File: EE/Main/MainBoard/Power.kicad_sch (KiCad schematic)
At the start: 31 parts, among them J8 Conn_01x02_Male, P1 USB_C_Plug_USB2.0, SW1 EG1206A, U2 LM3670MF-3.3, U4 MCP73832-2-OT, U5 MCP1640Cx-xCHY

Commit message: First pass layout
Assumes using Cut-through RGB 7 Segment
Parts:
- renumbered TP+ to TP+1, TP- to TP-1, TPVBAT to TPVBAT1, TPVBUS to TPVBUS1, TPVCC to TPVCC1, TPVd to TPVd1
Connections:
- net V_PRE_REG renamed VBAT_ADC
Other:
- note removed: "TODO Need to boost back up to 3.9V"
- note removed: "TODO math for resistors"
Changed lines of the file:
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@@
 		)
 	)
-	(text "TODO Need to boost back up to 3.9V"
-		(exclude_from_sim no)
-		(at 233.934 82.55 0)
-		(effects
-			(font
-				(size 1.27 1.27)
-			)
-		)
-	)
 	(text "Regulators"
 		(exclude_from_sim no)
@@
 		)
 	)
-	(text "TODO math for resistors"
-		(exclude_from_sim no)
-		(at 245.872 149.098 0)
-		(effects
-			(font
-				(size 1.27 1.27)
-			)
-		)
-	)
 	(label "VBAT"
 		(at 66.04 84.582 0)
@@
 		)
 	)
-	(label "V_DISPLAY"
-		(at 269.24 18.542 180)
+	(label "V_PRE_REG"
+		(at 138.43 81.28 0)
+		(fields_autoplaced yes)
+		(effects
+			(font
+				(size 1.27 1.27)
+			)
+			(justify left bottom)
+		)
+	)
+	(label "ADC_"
+		(at 270.51 24.13 180)
 		(fields_autoplaced yes)
 		(effects
@@
 		)
 	)
+	(label "ADC_"
+		(at 138.43 81.28 180)
+		(fields_autoplaced yes)
+		(effects
+			(font
+				(size 1.27 1.27)
+			)
+			(justify right bottom)
+		)
+	)
 	(label "VBAT"
 		(at 151.13 128.27 270)
@@
 		)
 	)
-	(hierarchical_label "V_DISPLAY"
+	(hierarchical_label "VBAT_ADC"
 		(shape input)
-		(at 269.24 18.542 0)
+		(at 270.51 24.13 0)
 		(fields_autoplaced yes)
 		(effects
@@
 		(dnp no)
 		(fields_autoplaced yes)
-		(property "Reference" "TP+"
+		(property "Reference" "TP+1"
 			(at 142.748 122.2205 90)
 			(effects
@@
 			(project ""
 				(path "/dfe0084c-a900-4f47-8966-915ebf3a8e75/d7ae3dec-973e-4961-81aa-d99c06a6b362"
-					(reference "TP+")
+					(reference "TP+1")
 					(unit 1)
 				)
@@
 		(on_board yes)
 		(dnp no)
-		(property "Reference" "TPVd"
+		(property "Reference" "TPVd1"
 			(at 274.574 106.934 0)
 			(effects
@@
 			(project "MainBoard"
 				(path "/dfe0084c-a900-4f47-8966-915ebf3a8e75/d7ae3dec-973e-4961-81aa-d99c06a6b362"
-					(reference "TPVd")
+					(reference "TPVd1")
 					(unit 1)
 				)
@@
 		(on_board yes)
 		(dnp no)
-		(property "Reference" "TPVCC"
+		(property "Reference" "TPVCC1"
 			(at 249.174 37.084 0)
 			(effects
@@
 			(project "MainBoard"
 				(path "/dfe0084c-a900-4f47-8966-915ebf3a8e75/d7ae3dec-973e-4961-81aa-d99c06a6b362"
-					(reference "TPVCC")
+					(reference "TPVCC1")
 					(unit 1)
 				)
@@
 		(dnp no)
 		(fields_autoplaced yes)
-		(property "Reference" "TP-"
+		(property "Reference" "TP-1"
 			(at 162.179 115.6278 90)
 			(effects
@@
 			(project ""
 				(path "/dfe0084c-a900-4f47-8966-915ebf3a8e75/d7ae3dec-973e-4961-81aa-d99c06a6b362"
-					(reference "TP-")
+					(reference "TP-1")
 					(unit 1)
 				)
@@
 		(dnp no)
 		(fields_autoplaced yes)
-		(property "Reference" "TPVBUS"
+		(property "Reference" "TPVBUS1"
 			(at 41.529 59.7478 90)
 			(effects
@@
 			(project "MainBoard"
 				(path "/dfe0084c-a900-4f47-8966-915ebf3a8e75/d7ae3dec-973e-4961-81aa-d99c06a6b362"
-					(reference "TPVBUS")
+					(reference "TPVBUS1")
 					(unit 1)
 				)
@@
 		(dnp no)
 		(fields_autoplaced yes)
-		(property "Reference" "TPVBAT"
+		(property "Reference" "TPVBAT1"
 			(at 77.089 59.7478 90)
 			(effects
@@
 			(project "MainBoard"
 				(path "/dfe0084c-a900-4f47-8966-915ebf3a8e75/d7ae3dec-973e-4961-81aa-d99c06a6b362"
-					(reference "TPVBAT")
+					(reference "TPVBAT1")
 					(unit 1)
 				)

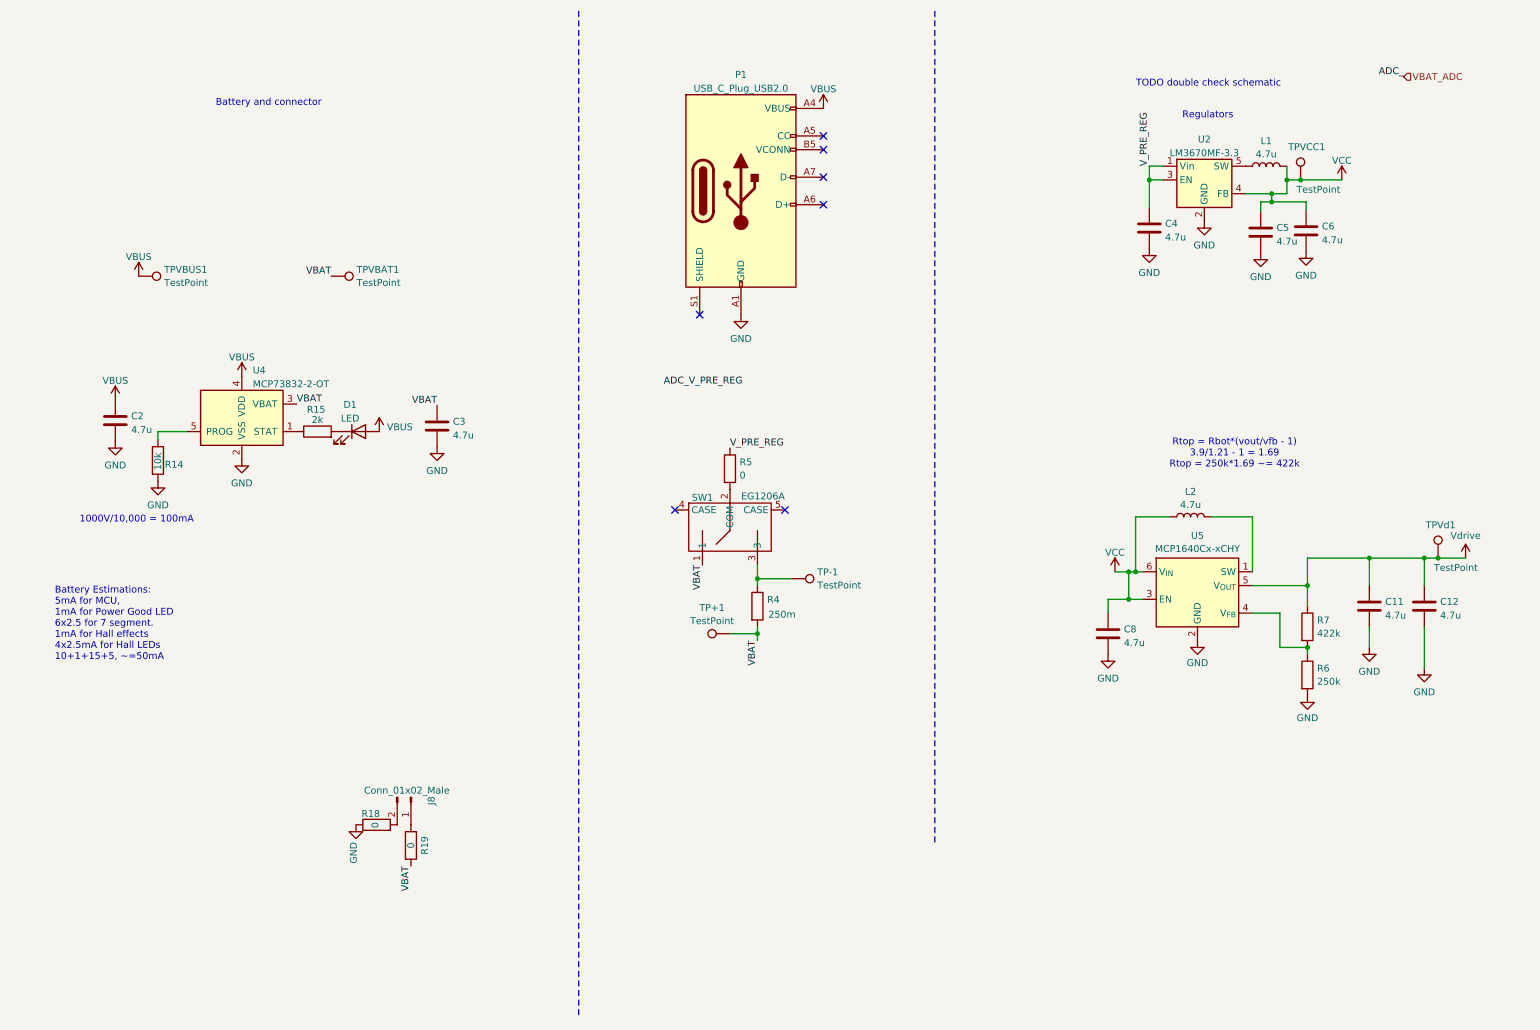
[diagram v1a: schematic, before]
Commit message: MCU Modification
Migrated to g431, as is used elsewhere.
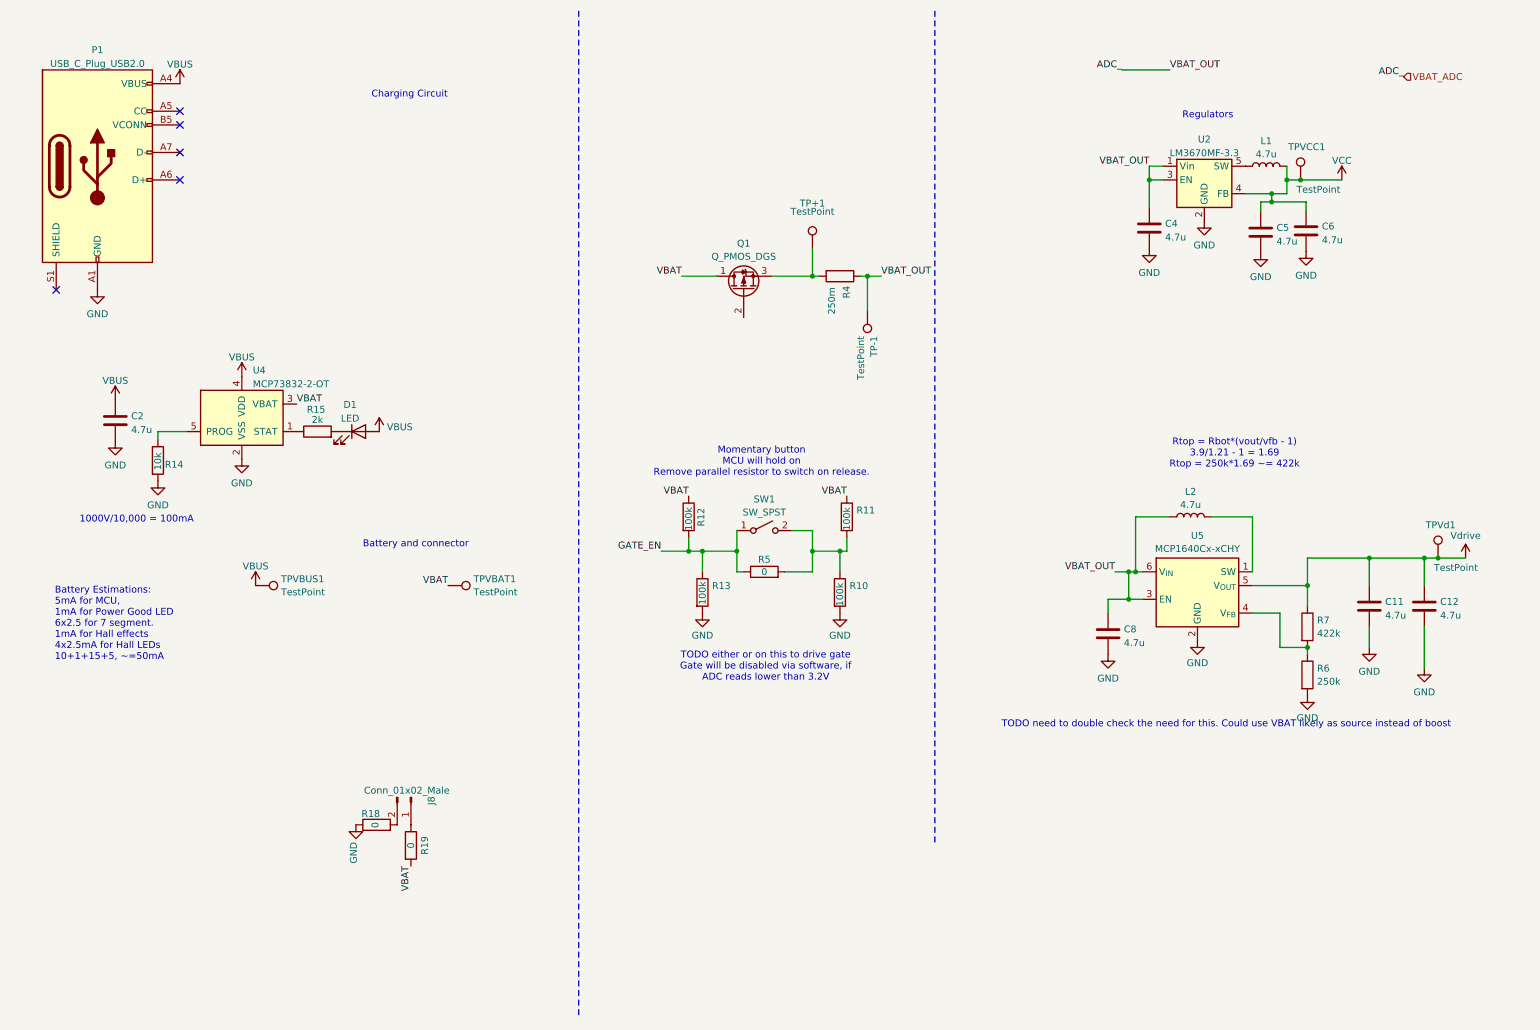
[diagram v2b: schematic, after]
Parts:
- removed C3: 4.7u, Capacitor_SMD:C_0603_1608Metric, symbol Device:C
- removed SW1: EG1206A, Library:EG1206A_EWI, symbol New_Library:EG1206A
- added Q1: Q_PMOS_DGS, symbol Device:Q_PMOS_DGS
- added R10, R11, R12, R13: 100k, symbol Device:R
- added SW1: SW_SPST, symbol Switch:SW_SPST
- R5: footprint Resistor_SMD:R_0402_1005Metric_Pad0.72x0.64mm_HandSolder -> (none)
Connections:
- net GND: now also R10.2, R13.2
- net VBAT: now also Q1.1 (D), R11.1, R12.1; no longer R4.2, TP+1.1
- net VBAT_ADC: now also C8.1, L2.1, R4.1, TP-1.1, U5.3 (EN), U5.6 (V_{IN}); no longer R5.1
- net VCC: no longer C8.1, L2.1, U5.3 (EN), U5.6 (V_{IN})
- net at R5.2: now also R10.1, R11.2, SW1.2 (B)
- new net: Q1.3 (S), R4.2, TP+1.1
- new net GATE_EN: R12.2, R13.1, R5.1, SW1.1 (A)
- no-connect marks 7 -> 5
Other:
- note added: "Charging Circuit"
- note added: "Momentary button MCU will hold on Remove parallel resistor to switch on release."
- note added: "TODO either or on this to drive gate Gate will be disabled via software, if ADC reads lower than 3.2V"
- note added: "TODO need to double check the need for this. Could use VBAT likely as source instead of boost"
- note removed: "TODO double check schematic"
- moved on the sheet: P1, R4, TP+1, TP-1, TPVBAT1, TPVBUS1

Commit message: Routine Checkout
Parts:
- removed C12: 4.7u, Capacitor_SMD:C_0603_1608Metric, symbol Device:C
- removed Q1: Q_PMOS_DGS, symbol Device:Q_PMOS_DGS
- removed R19: 0, Resistor_SMD:R_0402_1005Metric, symbol Device:R
- removed SW1: SW_SPST, symbol Switch:SW_SPST
- removed TPVBAT1, TPVBUS1, TPVd1: TestPoint, TestPoint:TestPoint_Pad_1.5x1.5mm, symbol Connector:TestPoint
- removed U2: LM3670MF-3.3, Package_TO_SOT_SMD:TSOT-23-5, symbol Regulator_Switching:LM3670MF
- removed U4: MCP73832-2-OT, Package_TO_SOT_SMD:SOT-23-5, symbol Battery_Management:MCP73832-2-OT
- removed U5: MCP1640Cx-xCHY, Package_TO_SOT_SMD:SOT-23-6, symbol Regulator_Switching:MCP1640Cx-xCHY
- added Q1: Q_PMOS_GSD, Package_TO_SOT_SMD:SOT-23, symbol Device:Q_PMOS_GSD
- added Q2: Q_NMOS_GSD, Package_TO_SOT_SMD:SOT-23, symbol Device:Q_NMOS_GSD
- added R21, R22: 10k, Resistor_SMD:R_0402_1005Metric, symbol Device:R
- added R23: 550k, Resistor_SMD:R_0402_1005Metric, symbol Device:R
- added R24: 100k, Resistor_SMD:R_0402_1005Metric, symbol Device:R
- added R25, R26: 1M, Resistor_SMD:R_0402_1005Metric, symbol Device:R
- added SW1: SW_DPST, symbol Switch:SW_DPST
- added TP3v1, TPPGate1: TestPoint, TestPoint:TestPoint_Pad_1.5x1.5mm, symbol Connector:TestPoint
- added U2: MCP73832-2-OT, Package_TO_SOT_SMD:SOT-23-5, symbol Battery_Management:MCP73832-2-OT
- added U4: ~, Package_TO_SOT_SMD:SOT-583-8, symbol library:TPS61033
- added U5: LM3670MF-3.3, Package_TO_SOT_SMD:TSOT-23-5, symbol Regulator_Switching:LM3670MF
- L1: value 4.7u -> 0.47u; P/N 74479775222A -> (none)
- R10, R13: value 100k -> 10k; footprint (none) -> Resistor_SMD:R_0402_1005Metric
- R11: value 100k -> 0; footprint (none) -> Resistor_SMD:R_0402_1005Metric
- R12: value 100k -> 250m; footprint (none) -> Resistor_SMD:R_0805_2012Metric
- R15: value 2k -> 10K
- R18: value 0 -> 10K
- R4: value 250m -> 10k; footprint Resistor_SMD:R_0805_2012Metric -> Resistor_SMD:R_0402_1005Metric
- R5: value 0 -> 4.7k; footprint (none) -> Resistor_SMD:R_0402_1005Metric
- R6: value 250k -> 1M; footprint (none) -> Resistor_SMD:R_0402_1005Metric
- R7: value 422k -> 0; footprint (none) -> Resistor_SMD:R_0402_1005Metric
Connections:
- net GATE_EN: now also R6.2, Q1.1 (G), Q2.3 (D), SW1.3, TPPGate1.1; no longer R12.2, R13.1, R5.1
- net GND: now also C5.1, R4.2, R7.1, R21.2, R24.2, R25.2, R26.2, U2.2 (VSS), U4.6 (GND), U5.2 (GND); no longer C5.2, R18.1, R6.2
- net VBAT: now also R11.2, R6.1, Q1.2 (S), U2.3 (VBAT); no longer R11.1, R12.1
- net VBAT_ADC: now also C5.2, L1.1, R12.1, U4.1 (VIN), U5.1 (Vin), U5.3 (EN); no longer C8.1, L2.1, R4.1
- net VBUS: now also U2.4 (VDD)
- net at J8.2 (Pin_2): now also R7.2; no longer R18.2
- net P_DRAIN: now reaches TP+1.1
- net P_DRAIN: now also R12.2, Q1.3 (D); no longer R4.2
- net at D1.1 (K): now also R5.2; no longer R15.2
- net N_SOURCE: now reaches R14.1
- net N_SOURCE: now also Q2.2 (S)
- net +3V3: now reaches L2.2
- net +3V3: now also C6.1, C8.1, R15.1, R18.1, TPVCC1.1, R25.1, SW1.1, U5.4 (FB)
- net at J8.1 (Pin_1): now also R11.1
- removed net VCC: C5.1, C6.1, L1.2, TPVCC1.1
- net Vdrive renamed 3v9
- net 3v9: now also R22.1, R23.1, R26.1, TP3v1.1, U4.8 (VOUT); no longer R7.1
- new net: R23.2, R24.1, U4.5 (FB)
- new net: L2.1, U5.5 (SW)
- new net: R22.2, U4.4 (PG)
- new net: R10.1, SW1.4
- new net: R4.1, U2.5 (PROG)
- new net: R5.1, U2.1 (STAT)
- new net: L1.2, U4.7 (SW)
- new net BTN_SNS: SW1.2
- new net EN: R18.2, U4.2 (EN)
- new net MODE: R21.1, U4.3 (MODE)
- new net N_GATE: Q2.1 (G), R13.1, R15.2
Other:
- note added: "R20= (Vout/vref-1)*R19 R20= (3.9/0.6-1)*100k R20 = 550k"
- note removed: "1000V/10,000 = 100mA"
- note removed: "Battery Estimations: 5mA for MCU, 1mA for Power Good LED 6x2.5 for 7 segment. 1mA for Hall effects 4x2.5mA for Hall LEDs 10+1+15+5, ~=50mA"
- note removed: "Battery and connector"
- note removed: "Charging Circuit"
- note removed: "Regulators"
- note removed: "Rtop = Rbot*(vout/vfb - 1) 3.9/1.21 - 1 = 1.69 Rtop = 250k*1.69 ~= 422k"
- note removed: "TODO either or on this to drive gate Gate will be disabled via software, if ADC reads lower than 3.2V"
- note removed: "TODO need to double check the need for this. Could use VBAT likely as source instead of boost"

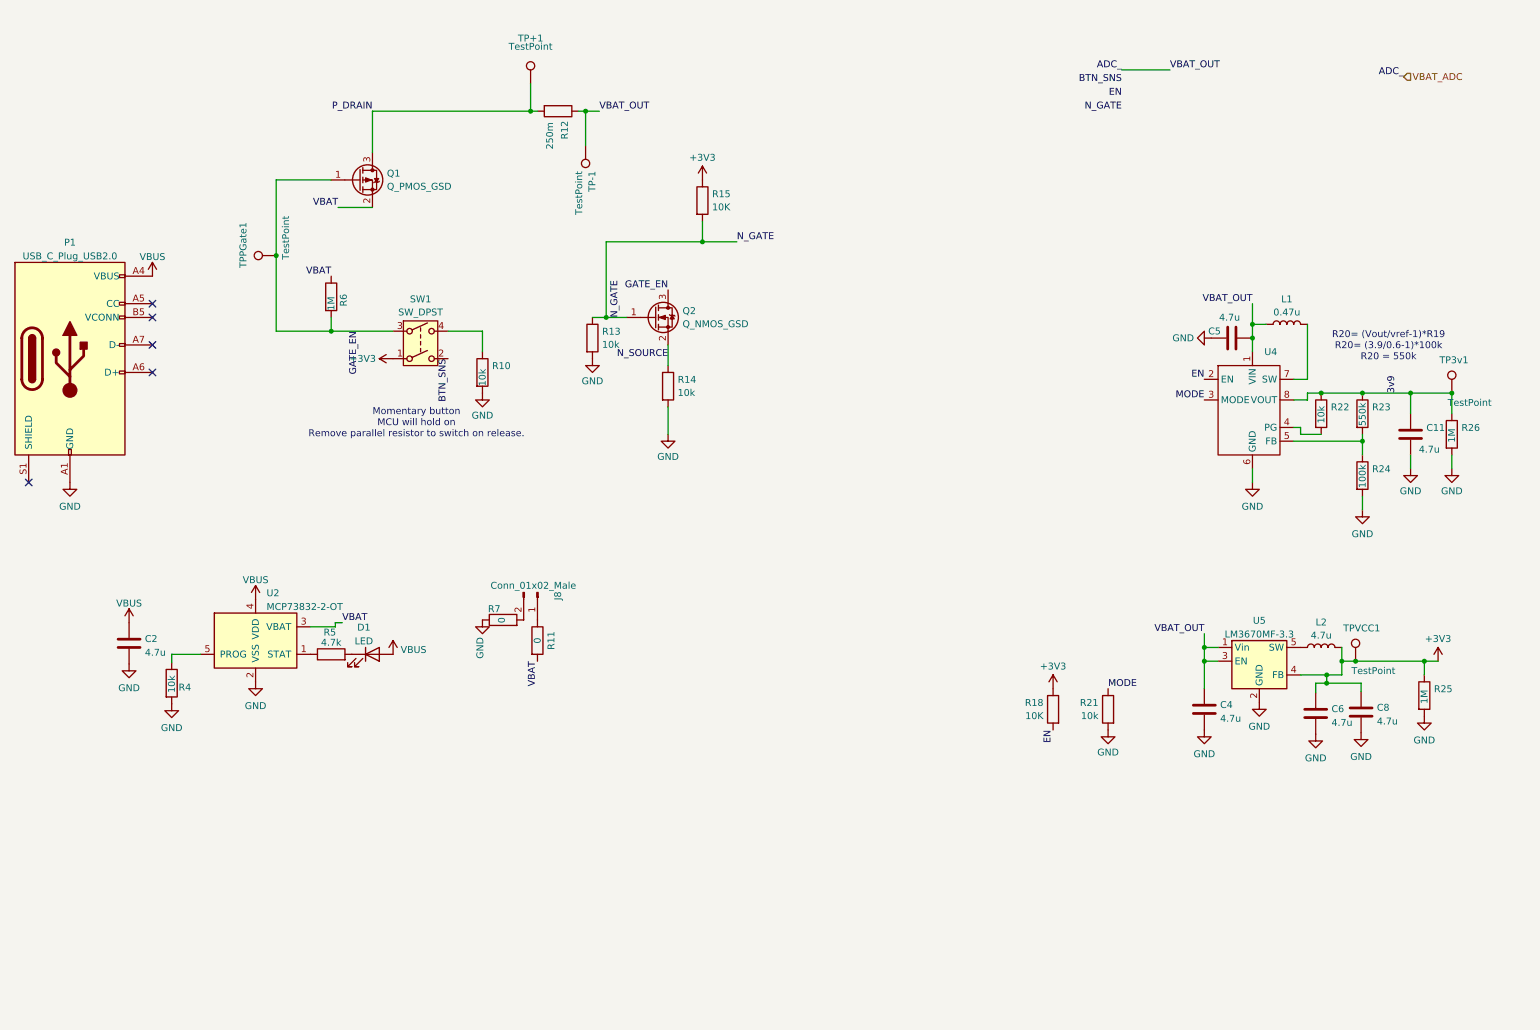
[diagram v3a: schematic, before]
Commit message: Potential Layout. Need to confirm button and L&F.
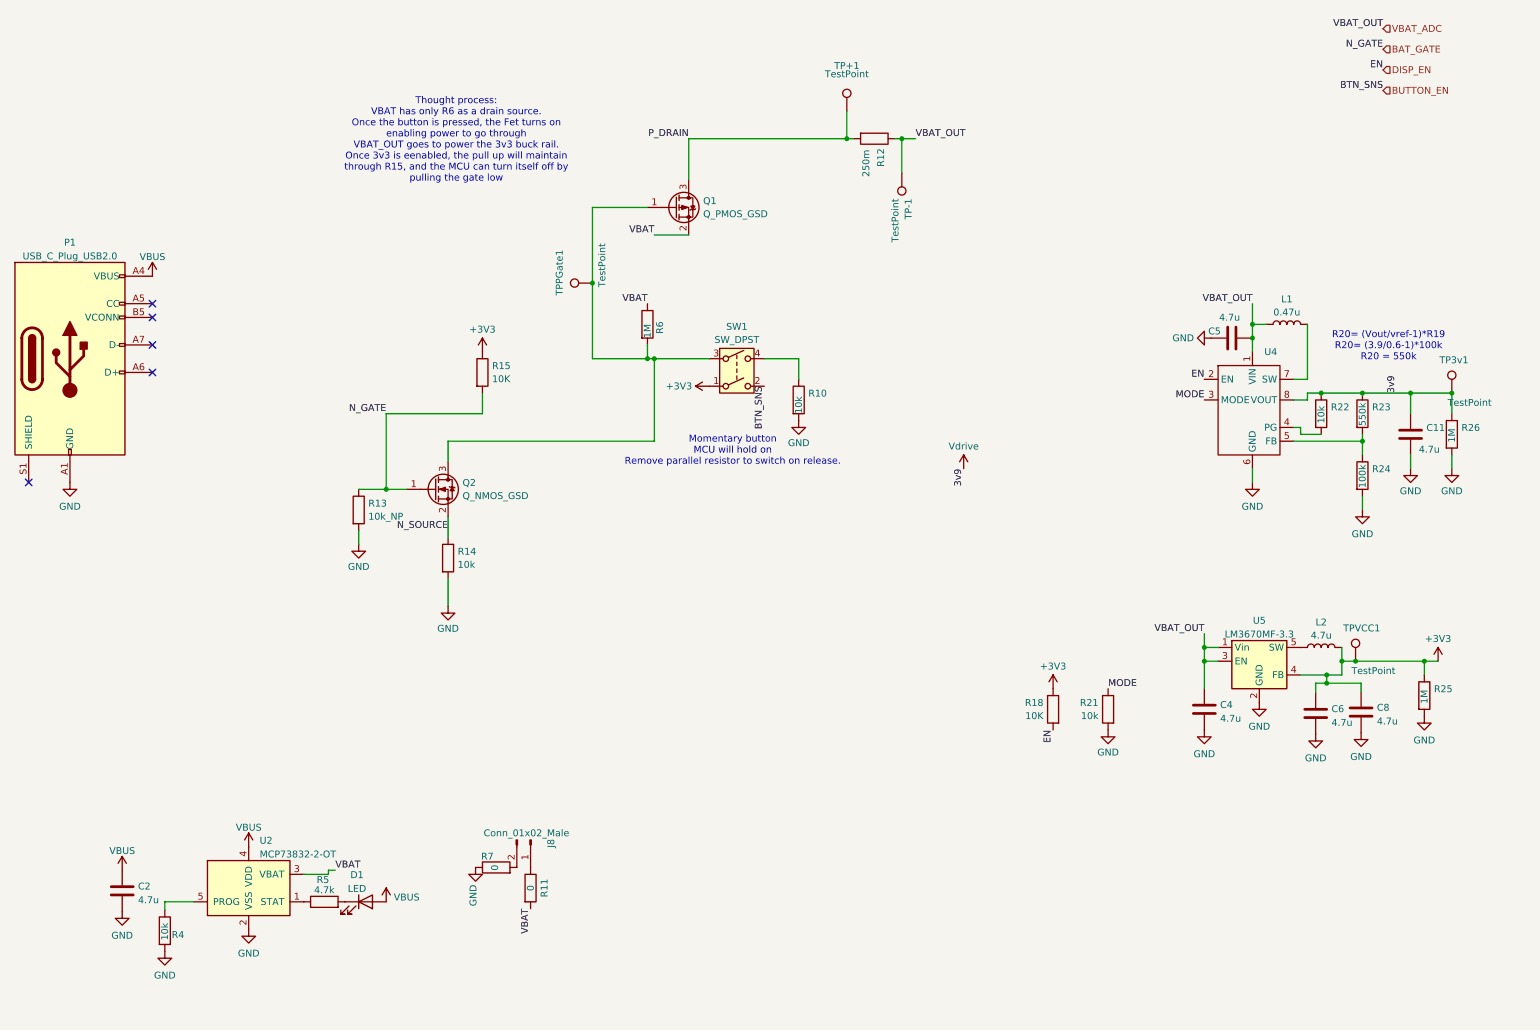
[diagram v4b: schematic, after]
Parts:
- R13: value 10k -> 10k_NP
- SW1: footprint (none) -> Library:401-1133-ND
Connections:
- net 3v9 renamed Vdrive
- net BTN_SNS renamed BUTTON_EN
- net EN renamed DISP_EN
- net GATE_EN: no longer names the net of Q1.1 (G), Q2.3 (D), R6.2, SW1.3, TPPGate1.1
- net N_GATE renamed BAT_GATE
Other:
- note added: "Thought process: VBAT has only R6 as a drain source. Once the button is pressed, the Fet turns on enabling power to go through VBAT_OUT goes to power the 3v3 buck rail. Once 3v3 is eenabled, the pull up will maintain through R15, and the MCU can turn itself off by pulling the gate low"
- moved on the sheet: C2, D1, J8, Q1, Q2, R10, R11, R12, R13, R14, R15, R4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
